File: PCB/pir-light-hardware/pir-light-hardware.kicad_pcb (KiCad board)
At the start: 2 copper layers, 25.8 x 18.9 mm, 3 parts, among them Q1 NMOS

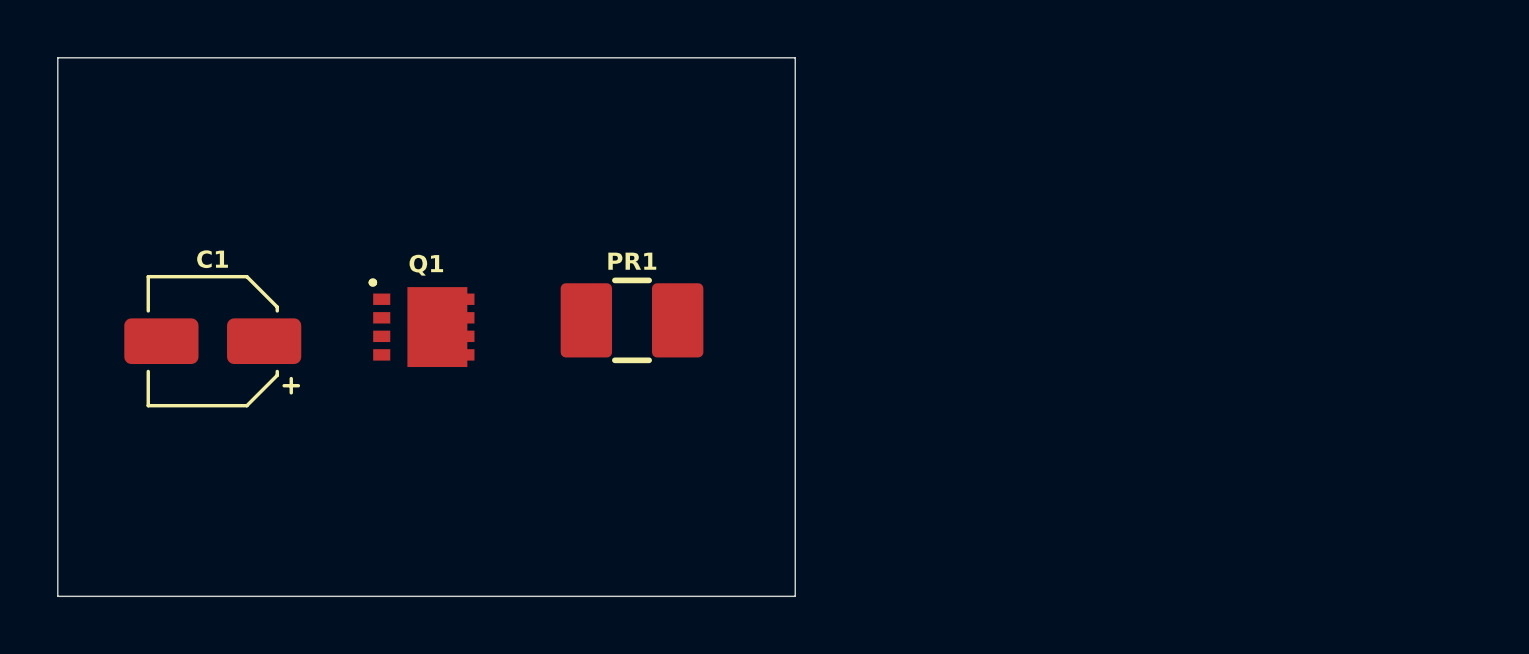
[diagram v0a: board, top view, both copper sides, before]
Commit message: chore(kicad): add final part of component libraries
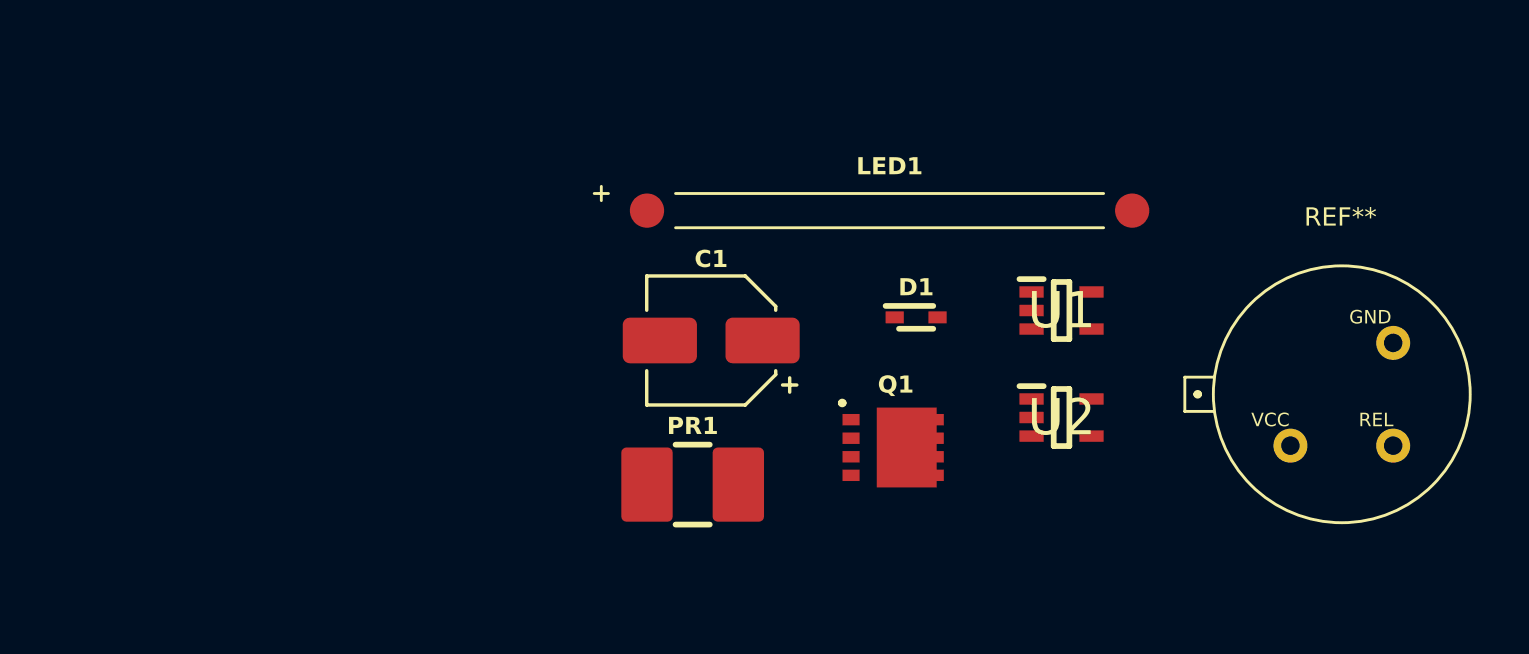
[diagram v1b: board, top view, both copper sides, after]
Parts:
- added D1: 1N5819HWQ-7-F, 1N5819HWQ-7-F:1N5819HWQ-7-F, F.Cu at (169.3, 90.4)
- added LED1: ~, LED-ROD:LED-ROD, F.Cu at (168.4, 86.7)
- added REF**: AS312-NEW, AS312:AS312-NEW, F.Cu at (182.4, 94.9)
- added U1: M74VHC1GT08DFT2G, M74VHC1GT08D:SOT65P210X110-5N, F.Cu at (174.4, 90.2)
- added U2: LMV331IDCKR, M74VHC1GT08D:SOT65P210X110-5N, F.Cu at (174.4, 93.9)
- moved C1 17.5 mm to (162.1, 91.2)
- moved Q1 17.0 mm to (168.6, 95.0)
- moved PR1 6.13 mm to (161.5, 96.3)
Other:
- board outline removed
